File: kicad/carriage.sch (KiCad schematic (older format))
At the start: 47 parts, among them CON10 Stepstick_Left_Connector, CON11 Stepstick_Right_Connector, CON12 Stepstick_Left_Connector, CON13 Stepstick_Right_Connector, CON14 Stepstick_Left_Connector, CON15 Stepstick_Right_Connector, CON9 Carriage, Q1 IRLR2905ZPBF, Q2 IRLR2905ZPBF, Q3 FDC6401N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

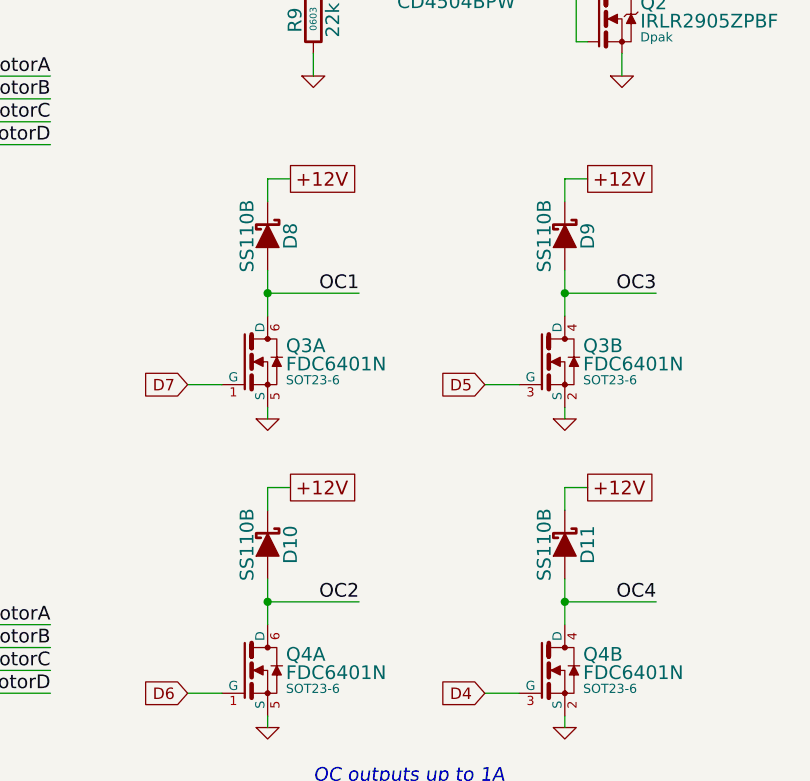
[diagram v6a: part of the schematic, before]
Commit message: Change 1A diodes. Add capacitors next to OC outputs. Place.
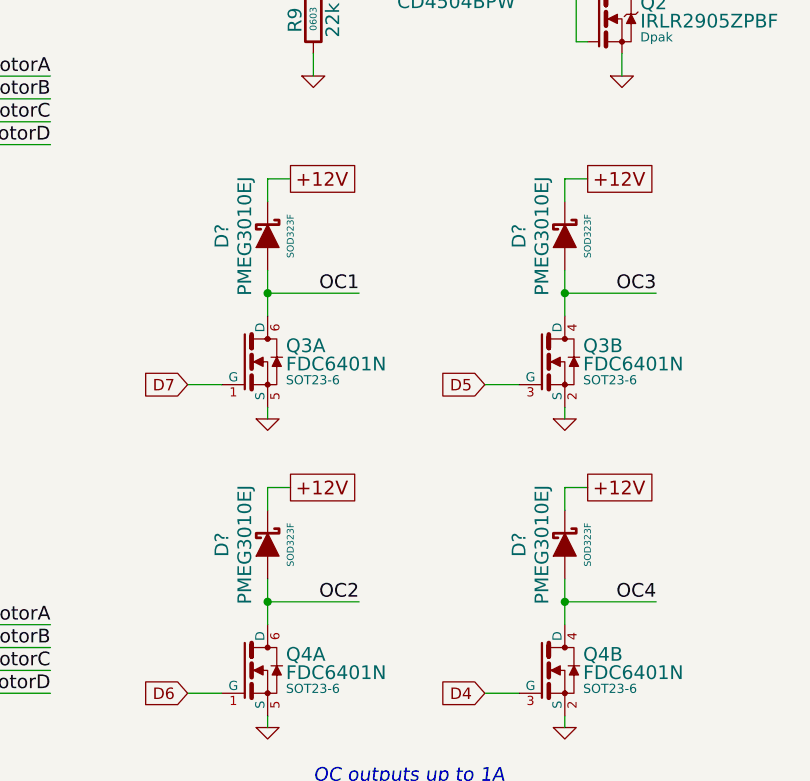
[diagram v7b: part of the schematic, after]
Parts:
- removed D10, D11, D8, D9: SS110B, symbol SS110B
- added D? (x4): PMEG3010EJ, SOD323F, symbol PMEG3010EJ
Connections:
- net +12V: now also D?.1, D?.1, D?.1, D?.1
- net OC1: now also D?.2
- net OC2: now also D?.2
- net OC3: now also D?.2
- net OC4: now also D?.2
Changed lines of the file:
@@
 	1    0    0    -1
-$EndComp
-$Comp
-L SS110B D11
-U 1 1 539234D0
-P 5800 6000
-F 0 "D11" H 5800 5900 60  0000 C CNN
-F 1 "SS110B" H 5800 6090 60  0000 C CNN
-F 2 "" V 5650 5962 30  0000 C CNN
-F 3 "" V 5800 6000 60  0000 C CNN
-	1    5800 6000
-	0    -1   -1   0
 $EndComp
 Text GLabel 5900 4400 2    60   UnSpc ~ 0
 +12V
-$Comp
-L SS110B D9
-U 1 1 53923925
-P 5800 4650
-F 0 "D9" H 5800 4550 60  0000 C CNN
-F 1 "SS110B" H 5800 4740 60  0000 C CNN
-F 2 "" V 5650 4612 30  0000 C CNN
-F 3 "" V 5800 4650 60  0000 C CNN
-	1    5800 4650
-	0    -1   -1   0
-$EndComp
 Text GLabel 4600 4400 2    60   UnSpc ~ 0
 +12V
-$Comp
-L SS110B D8
-U 1 1 539239AC
-P 4500 4650
-F 0 "D8" H 4500 4550 60  0000 C CNN
-F 1 "SS110B" H 4500 4740 60  0000 C CNN
-F 2 "" V 4350 4612 30  0000 C CNN
-F 3 "" V 4500 4650 60  0000 C CNN
-	1    4500 4650
-	0    -1   -1   0
-$EndComp
 Text GLabel 4600 5750 2    60   UnSpc ~ 0
 +12V
-$Comp
-L SS110B D10
-U 1 1 53923A40
-P 4500 6000
-F 0 "D10" H 4500 5900 60  0000 C CNN
-F 1 "SS110B" H 4500 6090 60  0000 C CNN
-F 2 "" V 4350 5962 30  0000 C CNN
-F 3 "" V 4500 6000 60  0000 C CNN
-	1    4500 6000
-	0    -1   -1   0
-$EndComp
 Connection ~ 5800 4900
 Connection ~ 4500 4900
@@
 	1    0    0    -1
 $EndComp
+$Comp
+L PMEG3010EJ D?
+U 1 1 539CC2B2
+P 4500 4650
+F 0 "D?" H 4500 4850 60  0000 C CNN
+F 1 "PMEG3010EJ" H 4500 4750 60  0000 C CNN
+F 2 "SOD323F" H 4500 4550 30  0000 C CNN
+F 3 "" V 4500 4650 60  0000 C CNN
+	1    4500 4650
+	0    -1   -1   0
+$EndComp
+$Comp
+L PMEG3010EJ D?
+U 1 1 539CC6A9
+P 4500 6000
+F 0 "D?" H 4500 6200 60  0000 C CNN
+F 1 "PMEG3010EJ" H 4500 6100 60  0000 C CNN
+F 2 "SOD323F" H 4500 5900 30  0000 C CNN
+F 3 "" V 4500 6000 60  0000 C CNN
+	1    4500 6000
+	0    -1   -1   0
+$EndComp
+$Comp
+L PMEG3010EJ D?
+U 1 1 539CC707
+P 5800 6000
+F 0 "D?" H 5800 6200 60  0000 C CNN
+F 1 "PMEG3010EJ" H 5800 6100 60  0000 C CNN
+F 2 "SOD323F" H 5800 5900 30  0000 C CNN
+F 3 "" V 5800 6000 60  0000 C CNN
+	1    5800 6000
+	0    -1   -1   0
+$EndComp
+$Comp
+L PMEG3010EJ D?
+U 1 1 539CC776
+P 5800 4650
+F 0 "D?" H 5800 4850 60  0000 C CNN
+F 1 "PMEG3010EJ" H 5800 4750 60  0000 C CNN
+F 2 "SOD323F" H 5800 4550 30  0000 C CNN
+F 3 "" V 5800 4650 60  0000 C CNN
+	1    5800 4650
+	0    -1   -1   0
+$EndComp
 $EndSCHEMATC

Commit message: Place
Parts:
- added C24, C25: 100n/50V, 0603, symbol C
- gave numbers to parts that had none: 4
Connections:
- net +12V: now also C24.1, C25.1
- net GND: now also C24.2, C25.2
- net OC2: now also D9.2, Q3.4 (D); no longer D10.2, Q4.6 (D)
- net OC3: now also D10.2, Q4.6 (D); no longer D9.2, Q3.4 (D)
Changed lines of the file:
@@
 D34
 $Comp
-L GND #PWR04
+L GND #PWR12
 U 1 1 534C44E8
 P 6050 3950
-F 0 "#PWR04" H 6050 3950 30  0001 C CNN
+F 0 "#PWR12" H 6050 3950 30  0001 C CNN
 F 1 "GND" H 6050 3880 30  0001 C CNN
 F 2 "~" H 6050 3950 60  0000 C CNN
@@
 D9
 $Comp
-L GND #PWR05
+L GND #PWR6
 U 1 1 534D96C2
 P 6050 2100
-F 0 "#PWR05" H 6050 2100 30  0001 C CNN
+F 0 "#PWR6" H 6050 2100 30  0001 C CNN
 F 1 "GND" H 6050 2030 30  0001 C CNN
 F 2 "~" H 6050 2100 60  0000 C CNN
@@
 D10
 $Comp
-L GND #PWR06
+L GND #PWR5
 U 1 1 534D96EE
 P 4750 2100
-F 0 "#PWR06" H 4750 2100 30  0001 C CNN
+F 0 "#PWR5" H 4750 2100 30  0001 C CNN
 F 1 "GND" H 4750 2030 30  0001 C CNN
 F 2 "~" H 4750 2100 60  0000 C CNN
@@
 $EndComp
 $Comp
-L GND #PWR07
+L GND #PWR18
 U 1 1 534EDD0C
 P 9650 5350
-F 0 "#PWR07" H 9650 5350 30  0001 C CNN
+F 0 "#PWR18" H 9650 5350 30  0001 C CNN
 F 1 "GND" H 9650 5280 30  0001 C CNN
 F 2 "~" H 9650 5350 60  0000 C CNN
@@
 A13
 $Comp
-L GND #PWR08
+L GND #PWR23
 U 1 1 534EDD2B
 P 9650 6300
-F 0 "#PWR08" H 9650 6300 30  0001 C CNN
+F 0 "#PWR23" H 9650 6300 30  0001 C CNN
 F 1 "GND" H 9650 6230 30  0001 C CNN
 F 2 "~" H 9650 6300 60  0000 C CNN
@@
 +12V
 $Comp
-L GND #PWR09
+L GND #PWR7
 U 1 1 536FC9C8
 P 7800 2200
-F 0 "#PWR09" H 7800 2200 30  0001 C CNN
+F 0 "#PWR7" H 7800 2200 30  0001 C CNN
 F 1 "GND" H 7800 2130 30  0001 C CNN
 F 2 "~" H 7800 2200 60  0000 C CNN
@@
 $EndComp
 $Comp
-L GND #PWR010
+L GND #PWR4
 U 1 1 536FC9D3
 P 9850 1950
-F 0 "#PWR010" H 9850 1950 30  0001 C CNN
+F 0 "#PWR4" H 9850 1950 30  0001 C CNN
 F 1 "GND" H 9850 1880 30  0001 C CNN
 F 2 "~" H 9850 1950 60  0000 C CNN
@@
 Text Label 6200 6250 2    60   ~ 0
 OC4
-Text Label 4900 6250 2    60   ~ 0
+Text Label 6200 4900 2    60   ~ 0
 OC2
 Text Label 8550 4850 2    60   ~ 0
@@
 Text Label 4900 4900 2    60   ~ 0
 OC1
-Text Label 6200 4900 2    60   ~ 0
+Text Label 4900 6250 2    60   ~ 0
 OC3
 Text Label 8550 5800 2    60   ~ 0
@@
 D3
 $Comp
-L GND #PWR011
+L GND #PWR11
 U 1 1 536FECC5
 P 4700 3950
-F 0 "#PWR011" H 4700 3950 30  0001 C CNN
+F 0 "#PWR11" H 4700 3950 30  0001 C CNN
 F 1 "GND" H 4700 3880 30  0001 C CNN
 F 2 "~" H 4700 3950 60  0000 C CNN
@@
 $EndComp
 $Comp
-L GND #PWR012
+L GND #PWR17
 U 1 1 537E69CA
 P 7750 5350
-F 0 "#PWR012" H 7750 5350 30  0001 C CNN
+F 0 "#PWR17" H 7750 5350 30  0001 C CNN
 F 1 "GND" H 7750 5280 30  0001 C CNN
 F 2 "~" H 7750 5350 60  0000 C CNN
@@
 $EndComp
 $Comp
-L GND #PWR013
+L GND #PWR22
 U 1 1 537E6A07
 P 7750 6300
-F 0 "#PWR013" H 7750 6300 30  0001 C CNN
+F 0 "#PWR22" H 7750 6300 30  0001 C CNN
 F 1 "GND" H 7750 6230 30  0001 C CNN
 F 2 "~" H 7750 6300 60  0000 C CNN
@@
 $EndComp
 $Comp
-L GND #PWR014
+L GND #PWR19
 U 1 1 539228B4
 P 4500 5450
-F 0 "#PWR014" H 4500 5450 30  0001 C CNN
+F 0 "#PWR19" H 4500 5450 30  0001 C CNN
 F 1 "GND" H 4500 5380 30  0001 C CNN
 F 2 "~" H 4500 5450 60  0000 C CNN
@@
 $EndComp
 $Comp
-L GND #PWR015
+L GND #PWR24
 U 1 1 53922C93
 P 4500 6800
-F 0 "#PWR015" H 4500 6800 30  0001 C CNN
+F 0 "#PWR24" H 4500 6800 30  0001 C CNN
 F 1 "GND" H 4500 6730 30  0001 C CNN
 F 2 "~" H 4500 6800 60  0000 C CNN
@@
 $EndComp
 $Comp
-L GND #PWR016
+L GND #PWR20
 U 1 1 53922EC9
 P 5800 5450
-F 0 "#PWR016" H 5800 5450 30  0001 C CNN
+F 0 "#PWR20" H 5800 5450 30  0001 C CNN
 F 1 "GND" H 5800 5380 30  0001 C CNN
 F 2 "~" H 5800 5450 60  0000 C CNN
@@
 $EndComp
 $Comp
-L GND #PWR017
+L GND #PWR25
 U 1 1 53922EFB
 P 5800 6800
-F 0 "#PWR017" H 5800 6800 30  0001 C CNN
+F 0 "#PWR25" H 5800 6800 30  0001 C CNN
 F 1 "GND" H 5800 6730 30  0001 C CNN
 F 2 "~" H 5800 6800 60  0000 C CNN
@@
 	4500 5750 4500 5850
 Wire Wire Line
-	4600 5750 4500 5750
+	4050 5750 4600 5750
 Wire Wire Line
 	4500 4400 4500 4500
 Wire Wire Line
-	4600 4400 4500 4400
+	3950 4400 4600 4400
 Wire Wire Line
 	5800 4400 5800 4500
@@
 $EndComp
 $Comp
-L GND #PWR018
+L GND #PWR10
 U 1 1 536FB0A2
 P 2900 2500
-F 0 "#PWR018" H 2900 2500 30  0001 C CNN
+F 0 "#PWR10" H 2900 2500 30  0001 C CNN
 F 1 "GND" H 2900 2430 30  0001 C CNN
 F 2 "~" H 2900 2500 60  0000 C CNN
@@
 X
 $Comp
-L GND #PWR019
+L GND #PWR8
 U 1 1 534EC7A1
 P 1700 2500
-F 0 "#PWR019" H 1700 2500 30  0001 C CNN
+F 0 "#PWR8" H 1700 2500 30  0001 C CNN
 F 1 "GND" H 1700 2430 30  0001 C CNN
 F 2 "~" H 1700 2500 60  0000 C CNN
@@
 $EndComp
 $Comp
-L GND #PWR020
+L GND #PWR9
 U 1 1 534EC79B
 P 2700 2500
-F 0 "#PWR020" H 2700 2500 30  0001 C CNN
+F 0 "#PWR9" H 2700 2500 30  0001 C CNN
 F 1 "GND" H 2700 2430 30  0001 C CNN
 F 2 "~" H 2700 2500 60  0000 C CNN
@@
 $EndComp
 $Comp
-L GND #PWR021
+L GND #PWR16
 U 1 1 539A105B
 P 2900 4950
-F 0 "#PWR021" H 2900 4950 30  0001 C CNN
+F 0 "#PWR16" H 2900 4950 30  0001 C CNN
 F 1 "GND" H 2900 4880 30  0001 C CNN
 F 2 "~" H 2900 4950 60  0000 C CNN
@@
 E1
 $Comp
-L GND #PWR022
+L GND #PWR14
 U 1 1 539A1070
 P 1700 4950
-F 0 "#PWR022" H 1700 4950 30  0001 C CNN
+F 0 "#PWR14" H 1700 4950 30  0001 C CNN
 F 1 "GND" H 1700 4880 30  0001 C CNN
 F 2 "~" H 1700 4950 60  0000 C CNN
@@
 $EndComp
 $Comp
-L GND #PWR023
+L GND #PWR15
 U 1 1 539A1076
 P 2700 4950
-F 0 "#PWR023" H 2700 4950 30  0001 C CNN
+F 0 "#PWR15" H 2700 4950 30  0001 C CNN
 F 1 "GND" H 2700 4880 30  0001 C CNN
 F 2 "~" H 2700 4950 60  0000 C CNN
@@
 $EndComp
 $Comp
-L GND #PWR024
+L GND #PWR28
 U 1 1 539A14BE
 P 2900 7350
-F 0 "#PWR024" H 2900 7350 30  0001 C CNN
+F 0 "#PWR28" H 2900 7350 30  0001 C CNN
 F 1 "GND" H 2900 7280 30  0001 C CNN
 F 2 "~" H 2900 7350 60  0000 C CNN
@@
 E2
 $Comp
-L GND #PWR025
+L GND #PWR26
 U 1 1 539A14D3
 P 1700 7350
-F 0 "#PWR025" H 1700 7350 30  0001 C CNN
+F 0 "#PWR26" H 1700 7350 30  0001 C CNN
 F 1 "GND" H 1700 7280 30  0001 C CNN
 F 2 "~" H 1700 7350 60  0000 C CNN
@@
 $EndComp
 $Comp
-L GND #PWR026
+L GND #PWR27
 U 1 1 539A14D9
 P 2700 7350
-F 0 "#PWR026" H 2700 7350 30  0001 C CNN
+F 0 "#PWR27" H 2700 7350 30  0001 C CNN
 F 1 "GND" H 2700 7280 30  0001 C CNN
 F 2 "~" H 2700 7350 60  0000 C CNN
@@
 $EndComp
 $Comp
-L PMEG3010EJ D?
+L PMEG3010EJ D8
 U 1 1 539CC2B2
 P 4500 4650
-F 0 "D?" H 4500 4850 60  0000 C CNN
-F 1 "PMEG3010EJ" H 4500 4750 60  0000 C CNN
+F 0 "D8" H 4500 4850 60  0000 C CNN
+F 1 "PMEG3010EJ" H 4450 4750 60  0000 C CNN
 F 2 "SOD323F" H 4500 4550 30  0000 C CNN
 F 3 "" V 4500 4650 60  0000 C CNN
@@
 $EndComp
 $Comp
-L PMEG3010EJ D?
+L PMEG3010EJ D10
 U 1 1 539CC6A9
 P 4500 6000
-F 0 "D?" H 4500 6200 60  0000 C CNN
-F 1 "PMEG3010EJ" H 4500 6100 60  0000 C CNN
+F 0 "D10" H 4500 6200 60  0000 C CNN
+F 1 "PMEG3010EJ" H 4450 6100 60  0000 C CNN
 F 2 "SOD323F" H 4500 5900 30  0000 C CNN
 F 3 "" V 4500 6000 60  0000 C CNN
@@
 $EndComp
 $Comp
-L PMEG3010EJ D?
+L PMEG3010EJ D11
 U 1 1 539CC707
 P 5800 6000
-F 0 "D?" H 5800 6200 60  0000 C CNN
+F 0 "D11" H 5800 6200 60  0000 C CNN
 F 1 "PMEG3010EJ" H 5800 6100 60  0000 C CNN
 F 2 "SOD323F" H 5800 5900 30  0000 C CNN
@@
 $EndComp
 $Comp
-L PMEG3010EJ D?
+L PMEG3010EJ D9
 U 1 1 539CC776
 P 5800 4650
-F 0 "D?" H 5800 4850 60  0000 C CNN
+F 0 "D9" H 5800 4850 60  0000 C CNN
 F 1 "PMEG3010EJ" H 5800 4750 60  0000 C CNN
 F 2 "SOD323F" H 5800 4550 30  0000 C CNN
@@
 	0    -1   -1   0
 $EndComp
+$Comp
+L C C25
+U 1 1 539D0ECF
+P 4050 6000
+F 0 "C25" H 4055 6085 60  0000 L CNN
+F 1 "100n/50V" H 4056 5915 60  0000 L CNN
+F 2 "0603" H 4150 5850 30  0000 C CNN
+F 3 "~" H 4050 6000 60  0000 C CNN
+	1    4050 6000
+	-1   0    0    -1
+$EndComp
+Wire Wire Line
+	4050 5750 4050 5850
+Connection ~ 4500 5750
+Wire Wire Line
+	4050 6150 4050 6200
+$Comp
+L GND #PWR21
+U 1 1 539D1289
+P 4050 6200
+F 0 "#PWR21" H 4050 6200 30  0001 C CNN
+F 1 "GND" H 4050 6130 30  0001 C CNN
+F 2 "~" H 4050 6200 60  0000 C CNN
+F 3 "~" H 4050 6200 60  0000 C CNN
+	1    4050 6200
+	1    0    0    -1
+$EndComp
+$Comp
+L C C24
+U 1 1 539D12F3
+P 3950 4650
+F 0 "C24" H 3955 4735 60  0000 L CNN
+F 1 "100n/50V" H 3956 4565 60  0000 L CNN
+F 2 "0603" H 4050 4500 30  0000 C CNN
+F 3 "~" H 3950 4650 60  0000 C CNN
+	1    3950 4650
+	-1   0    0    -1
+$EndComp
+Wire Wire Line
+	3950 4400 3950 4500
+Wire Wire Line
+	3950 4800 3950 4850
+$Comp
+L GND #PWR13
+U 1 1 539D12FB
+P 3950 4850
+F 0 "#PWR13" H 3950 4850 30  0001 C CNN
+F 1 "GND" H 3950 4780 30  0001 C CNN
+F 2 "~" H 3950 4850 60  0000 C CNN
+F 3 "~" H 3950 4850 60  0000 C CNN
+	1    3950 4850
+	1    0    0    -1
+$EndComp
+Connection ~ 4500 4400
 $EndSCHEMATC
